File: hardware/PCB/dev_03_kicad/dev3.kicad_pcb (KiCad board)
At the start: 2 copper layers, 50.3 x 44.5 mm, 27 parts, among them P1 USB_OTG, P3 CONN_01X04, P4 Mic_IN, P5 MCP3201, P7 USB_OTG, P8 CONN_01X04, SW1 SW_PUSH, U1 ESP-07v2, U2 LM1117-3.3, U3 FT232RL

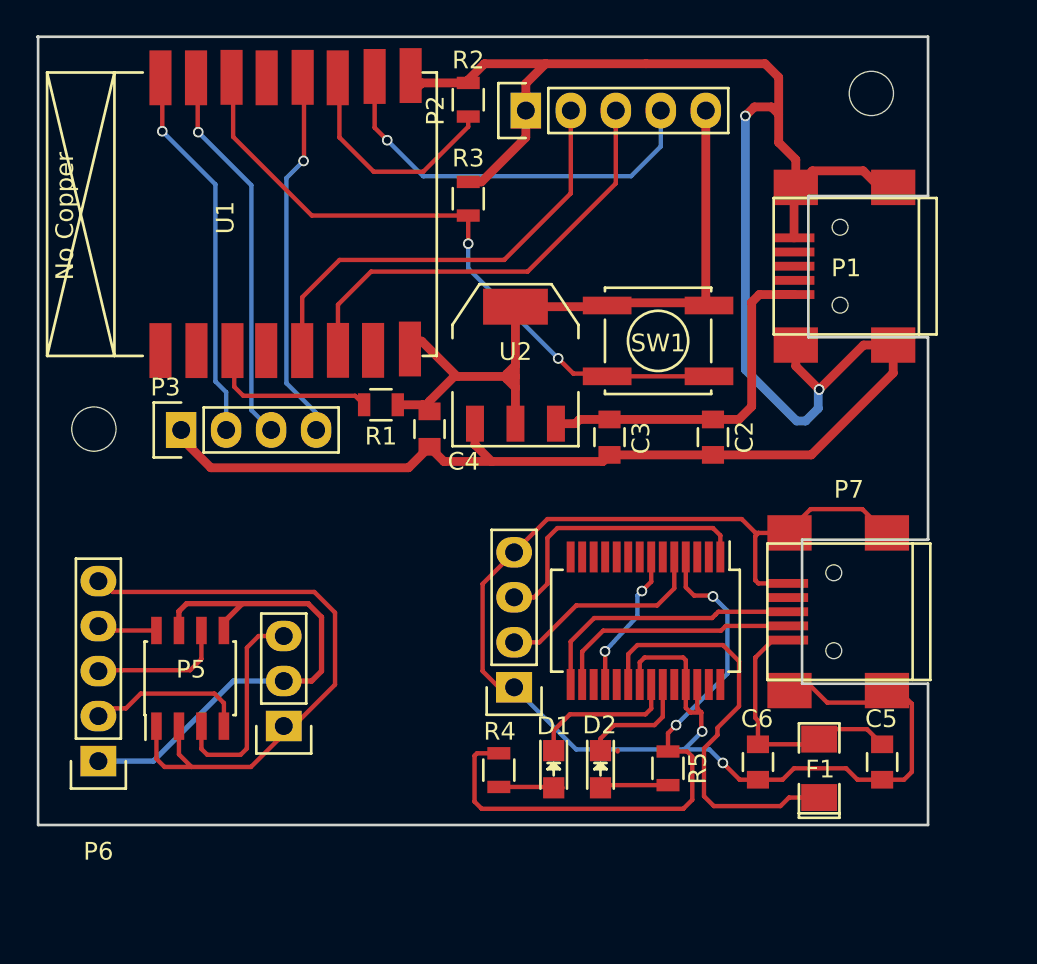
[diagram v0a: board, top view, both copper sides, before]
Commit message: PCB arbete och bilder
Fortsätter PCB, ny två paneler. Lite nya bilder tagna på arbetet.
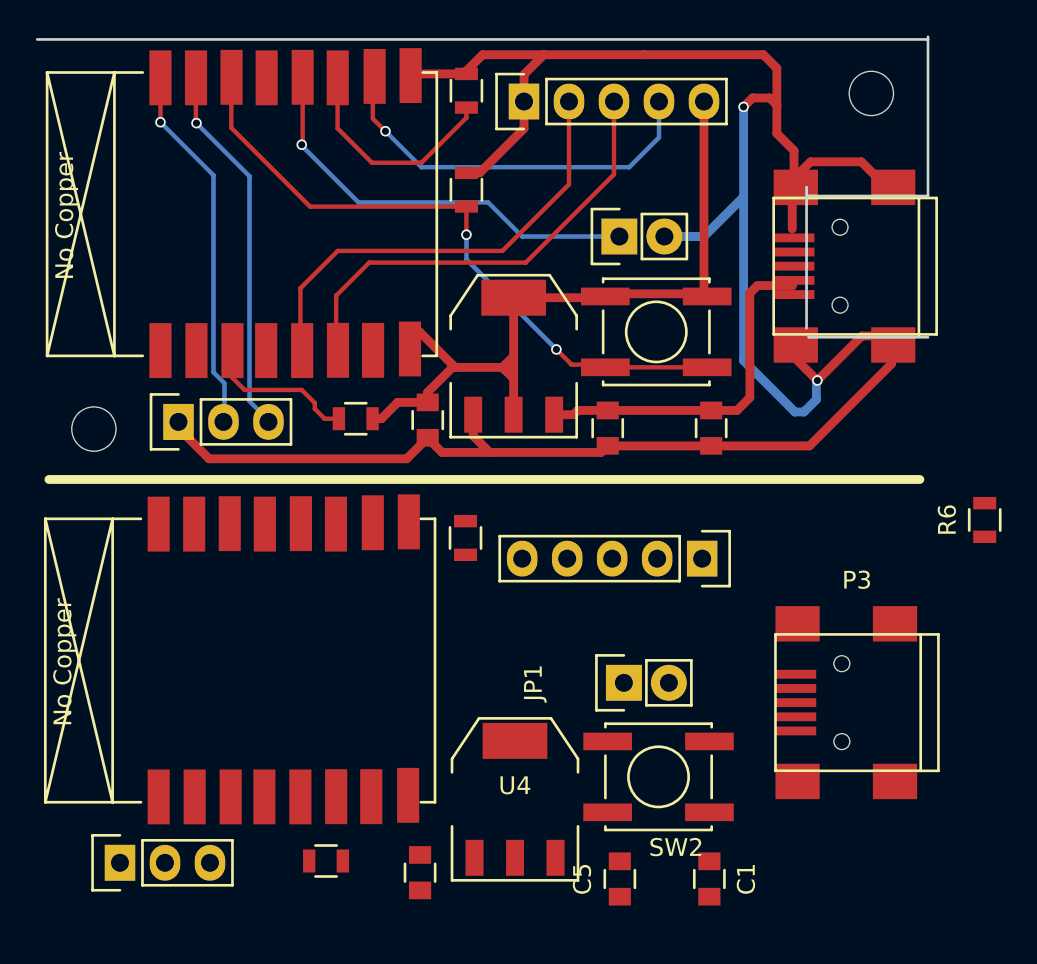
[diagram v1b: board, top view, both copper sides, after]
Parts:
- removed C6: C, Capacitors_SMD:C_0805
- removed D1, D2: LED, LEDs:LED_0805
- removed F1: F_Small, SMD_Packages:SMD-1206_Pol
- removed P4: Mic_IN, Pin_Headers:Pin_Header_Straight_1x03
- removed P5: MCP3201, Housings_SOIC:SOIC-8_3.9x4.9mm_Pitch1.27mm
- removed P6: , Pin_Headers:Pin_Header_Straight_1x05
- removed P7: USB_OTG, Connect:USB_Mini-B
- removed P8: CONN_01X04, Pin_Headers:Pin_Header_Straight_1x04
- removed R4, R5: 333, Resistors_SMD:R_0805
- removed U3: FT232RL, Housings_SSOP:SSOP-28_5.3x10.2mm_Pitch0.65mm
- added ?: 10uF, Capacitors_SMD:C_0805, F.Cu at (137.7, 130.3)
- added ?: , Pin_Headers:Pin_Header_Straight_1x02, F.Cu at (149.0, 94.3)
- added ?: , Pin_Headers:Pin_Header_Straight_1x05, F.Cu at (153.7, 112.5)
- added ?: CONN_01X03, Socket_Strips:Socket_Strip_Straight_1x03, F.Cu at (120.8, 129.7)
- added ?: , Socket_Strips:Socket_Strip_Straight_1x03, F.Cu at (124.1, 104.8)
- added ?: , Resistors_SMD:R_0805, F.Cu at (132.4, 129.6)
- added ?: , Resistors_SMD:R_0805, F.Cu at (140.3, 111.4)
- added ?: , dev_02_kicad:ESP-07v2, F.Cu at (123.0, 125.3)
- added C1: 0,1uF, Capacitors_SMD:C_0805, F.Cu at (154.1, 130.6)
- added JP1: JUMPER, Pin_Headers:Pin_Header_Straight_1x02, F.Cu at (149.3, 119.5)
- added R6: 10k, Resistors_SMD:R_0805, F.Cu at (169.6, 110.3)
- added SW2: SW_PUSH, Buttons_Switches_SMD:SW_SPST_EVPBF, F.Cu at (151.2, 124.8)
- added U4: LM1117-3.3, TO_SOT_Packages_SMD:SOT-223, F.Cu at (143.1, 126.1)
- ?: renamed from U1; value ESP-07v2 -> (none)
- C5: value C -> 10uF
- P3: value CONN_01X04 -> USB_OTG; footprint Pin_Headers:Pin_Header_Straight_1x04 -> Connect:USB_Mini-B
- moved P3 41.1 mm to (162.4, 120.7), turned to 180 degrees
- moved C5 16.2 mm to (149.0, 130.6)
- moved ? 1.63 mm to (134.1, 104.6)
- moved ? 0.52 mm to (143.6, 86.7)
- moved ? 0.52 mm to (140.4, 86.1)
- moved ? 0.52 mm to (138.2, 104.7)
- moved ? 0.52 mm to (151.1, 99.7)
- moved ? 0.52 mm to (154.2, 105.2)
- moved ? 0.52 mm to (148.3, 105.2)
- moved ? 0.52 mm to (140.4, 91.7)
- moved ? 0.52 mm to (143.0, 101.1)
- renumbered P1 to ?, P2 to ?, C2 to ?, C3 to ?, C4 to ?, R1 to ?, R2 to ?, R3 to ?, SW1 to ?, U2 to ?
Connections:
- ? pad 2: (no net) -> Net-(P1-Pad2)
- ? pad 3: (no net) -> Net-(P1-Pad3)
- ? pad 4: (no net) -> Net-(P1-Pad4)
- ? pad 1: (no net) -> Net-(U1-Pad1)
- ? pad 12: Net-(P3-Pad4) -> Net-(JP2-Pad1)
- ? pad 13: (no net) -> Net-(U1-Pad13)
- ? pad 2: (no net) -> Net-(U1-Pad2)
- ? pad 4: (no net) -> Net-(U1-Pad4)
- ? pad 7: (no net) -> Net-(U1-Pad7)
- C5 pad 2: Net-(C5-Pad2) -> +5VD
- P3 pad 1: GND -> +5VD
- P3 pad 2: RX -> Net-(P3-Pad2)
- P3 pad 3: TX -> Net-(P3-Pad3)
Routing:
- net GNDA: track 95.9 -> 0.00 mm, vias 4 -> 0
- net VCC_A: track 34.9 -> 0.00 mm
- net VCCIO: track 34.6 -> 0.00 mm, vias 2 -> 0
- net GNDD: track 29.3 -> 0.00 mm
- net Net-(F1-Pad1): track 27.0 -> 0.00 mm
- net Net-(JP2-Pad1): track 0.00 -> 23.2 mm, vias 0 -> 1
- net Net-(P3-Pad4): track 20.0 -> 0.00 mm, vias 1 -> 0
- net TX_A: track 16.2 -> 0.00 mm
- net USBDp: track 15.6 -> 0.00 mm
- net Net-(C5-Pad2): track 14.9 -> 0.00 mm
- net USBDm: track 14.3 -> 0.00 mm
- net AnalogIn: track 12.2 -> 0.00 mm
- net RX_A: track 12.1 -> 0.00 mm
- net SCLK_A: track 9.69 -> 0.00 mm
- net Net-(D1-Pad1): track 8.51 -> 0.00 mm
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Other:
- board size 50.3 x 44.5 mm -> 50.3 x 17 mm

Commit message: UDPModul - Logfunktion
UDPModul - Logfunktion
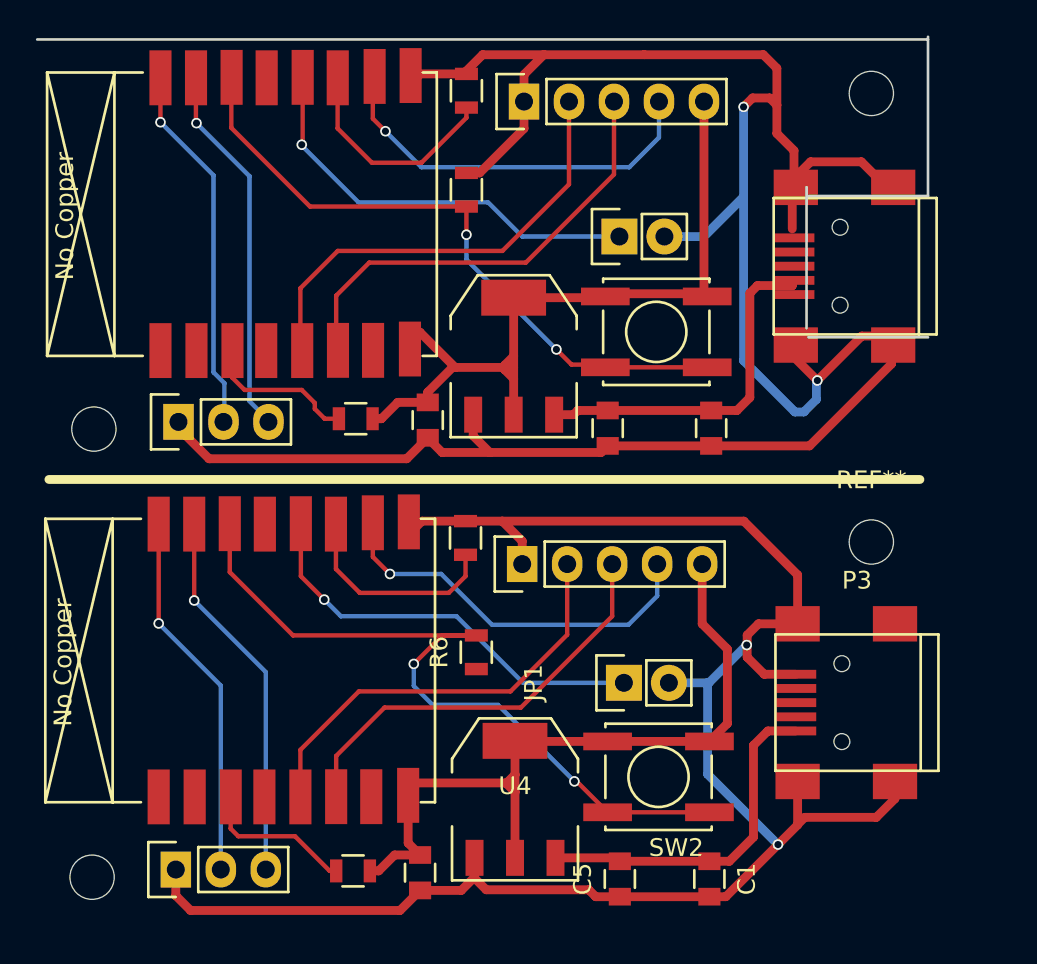
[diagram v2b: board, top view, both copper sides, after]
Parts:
- added ?: , Mounting_Holes:MountingHole_2.5mm, F.Cu at (119.2, 130.5)
- added REF**: MountingHole_2.5mm, Mounting_Holes:MountingHole_2.5mm, F.Cu at (163.2, 111.6)
- ?: value CONN_01X03 -> (none)
- moved R6 29.7 mm to (140.9, 117.8)
- moved ? 10.2 mm to (143.5, 112.8), turned to 90 degrees
- moved ? 3.17 mm to (124.0, 130.1)
- moved ? 1.62 mm to (134.0, 130.1)
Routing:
- net GNDA: track 0.00 -> 104.4 mm, vias 0 -> 2
- net +3.3VDAC: track 0.00 -> 43.7 mm
- net Net-(R6-Pad2): track 0.00 -> 42.5 mm, vias 0 -> 2
- net SCLK_2: track 0.00 -> 23.7 mm
- net MISO_2: track 0.00 -> 23.4 mm
- net Net-(JP1-Pad1): track 0.00 -> 23.0 mm, vias 0 -> 1
- net SS_2: track 0.00 -> 21.3 mm, vias 0 -> 1
- net TX_2: track 0.00 -> 20.5 mm, vias 0 -> 1
- net RX_2: track 0.00 -> 20.3 mm, vias 0 -> 1
- net +5VD: track 0.00 -> 19.7 mm
- net Net-(R5-Pad1): track 0.00 -> 11.3 mm
- net Net-(R4-Pad2): track 0.00 -> 9.44 mm

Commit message: UDPServer
Hela UDP Server projecktet
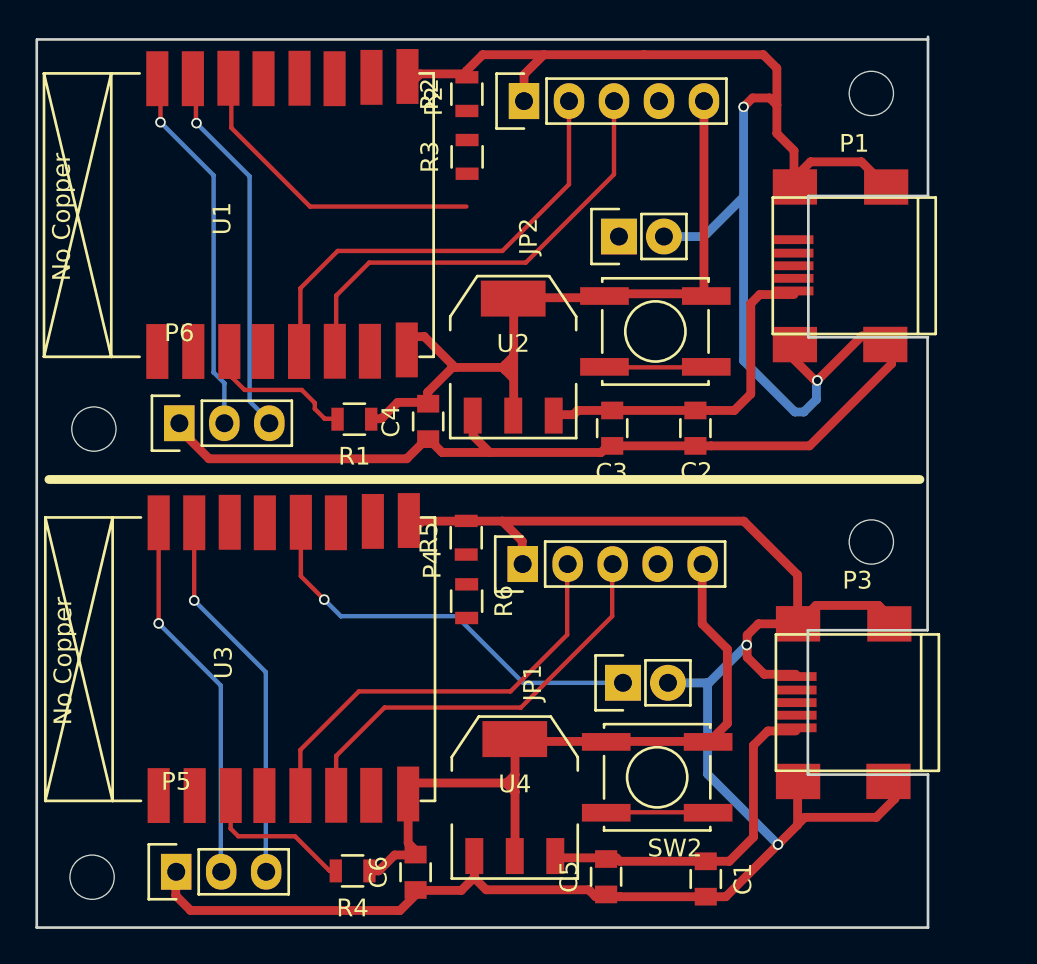
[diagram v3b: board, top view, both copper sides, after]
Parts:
- removed the ? at (162.3, 96.0)
- removed the ? at (123.1, 100.1)
- removed the ? at (143.6, 86.7)
- removed the ? at (137.7, 130.3)
- removed the ? at (149.0, 94.3)
- removed the ? at (143.5, 112.8)
- removed the ? at (124.0, 130.1)
- removed the ? at (124.1, 104.8)
- removed the ? at (134.0, 130.1)
- removed the ? at (154.2, 105.2)
- removed the ? at (140.3, 111.4)
- removed the ? at (123.0, 125.3)
- removed the ? at (148.3, 105.2)
- removed the ? at (138.2, 104.7)
- removed the ? at (134.1, 104.6)
- removed the ? at (140.4, 86.1)
- removed the ? at (140.4, 91.7)
- removed the ? at (151.1, 99.7)
- removed the ? at (143.0, 101.1)
- added C2: 0,1uF, Capacitors_SMD:C_0805, F.Cu at (153.3, 105.2)
- added C3: 10uF, Capacitors_SMD:C_0805, F.Cu at (148.6, 105.2)
- added C4: 10uF, Capacitors_SMD:C_0805, F.Cu at (138.2, 104.8)
- added C6: 10uF, Capacitors_SMD:C_0805, F.Cu at (137.5, 130.2)
- added JP2: JUMPER, Pin_Headers:Pin_Header_Straight_1x02, F.Cu at (149.0, 94.3)
- added P1: USB_OTG, ASKicadLib:USB_Mini-B_AS, F.Cu at (162.3, 96.0)
- added P2: Pinhead SMD Connector, Pin_Headers:Pin_Header_Straight_1x05, F.Cu at (143.6, 86.7)
- added P4: Pinhead SMD Connector, Pin_Headers:Pin_Header_Straight_1x05, F.Cu at (143.5, 112.8)
- added P5: CONN_01X03, Socket_Strips:Socket_Strip_Straight_1x03, F.Cu at (124.0, 130.2)
- added P6: CONN_01X03, Socket_Strips:Socket_Strip_Straight_1x03, F.Cu at (124.2, 104.9)
- added R1: 10k, Resistors_SMD:R_0805, F.Cu at (134.0, 104.6)
- added R2: 10k, Resistors_SMD:R_0805, F.Cu at (140.4, 86.3)
- added R3: 10k, Resistors_SMD:R_0805, F.Cu at (140.4, 89.8)
- added R4: 10k, Resistors_SMD:R_0805, F.Cu at (133.9, 130.1)
- added R5: 10k, Resistors_SMD:R_0805, F.Cu at (140.3, 111.3)
- added SW1: SW_PUSH, Buttons_Switches_SMD:SW_SPST_EVPBF, F.Cu at (151.0, 99.7)
- added U1: ESP-07v2, dev_02_kicad:ESP-07v2, F.Cu at (122.9, 100.1)
- added U2: LM1117-3.3, TO_SOT_Packages_SMD:SOT-223, F.Cu at (143.0, 101.1)
- added U3: ESP-07v2, dev_02_kicad:ESP-07v2, F.Cu at (123.0, 125.2)
- ?: renamed from REF**; value MountingHole_2.5mm -> (none)
- P3: footprint Connect:USB_Mini-B -> ASKicadLib:USB_Mini-B_AS
- moved R6 2.93 mm to (140.4, 114.9), turned to 270 degrees
- moved C5 0.79 mm to (148.2, 130.5)
- moved C1 0.20 mm to (153.9, 130.6)
- moved U4 0.10 mm to (143.1, 126.0)
- moved SW2 0.08 mm to (151.1, 124.9)
- moved JP1 0.05 mm to (149.2, 119.5)
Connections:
- P3 pad 2: Net-(P3-Pad2) -> (no net)
- P3 pad 3: Net-(P3-Pad3) -> (no net)
- P3 pad 4: Net-(P3-Pad4) -> (no net)
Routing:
- net Net-(R6-Pad2): track 42.5 -> 5.75 mm, vias 2 -> 0
- net Net-(JP2-Pad1): track 23.2 -> 0.00 mm, vias 1 -> 0
- net SS: track 22.2 -> 0.00 mm, vias 1 -> 0
- net SS_2: track 21.3 -> 0.00 mm, vias 1 -> 0
- net Net-(R3-Pad2): track 37.2 -> 23.2 mm, vias 2 -> 0
- net Net-(R2-Pad1): track 12.1 -> 0.00 mm
- net Net-(R5-Pad1): track 11.3 -> 0.00 mm
- net GND: track 131.8 -> 124.0 mm
- net GNDA: track 104.4 -> 110.8 mm
- net +5V: track 20.9 -> 19.3 mm
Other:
- board size 50.3 x 17 mm -> 50.3 x 50.3 mm
